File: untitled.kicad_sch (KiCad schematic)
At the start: 2 parts, among them J1 USB4056-03-A_REVA2, U1 STM32H745ZIT6

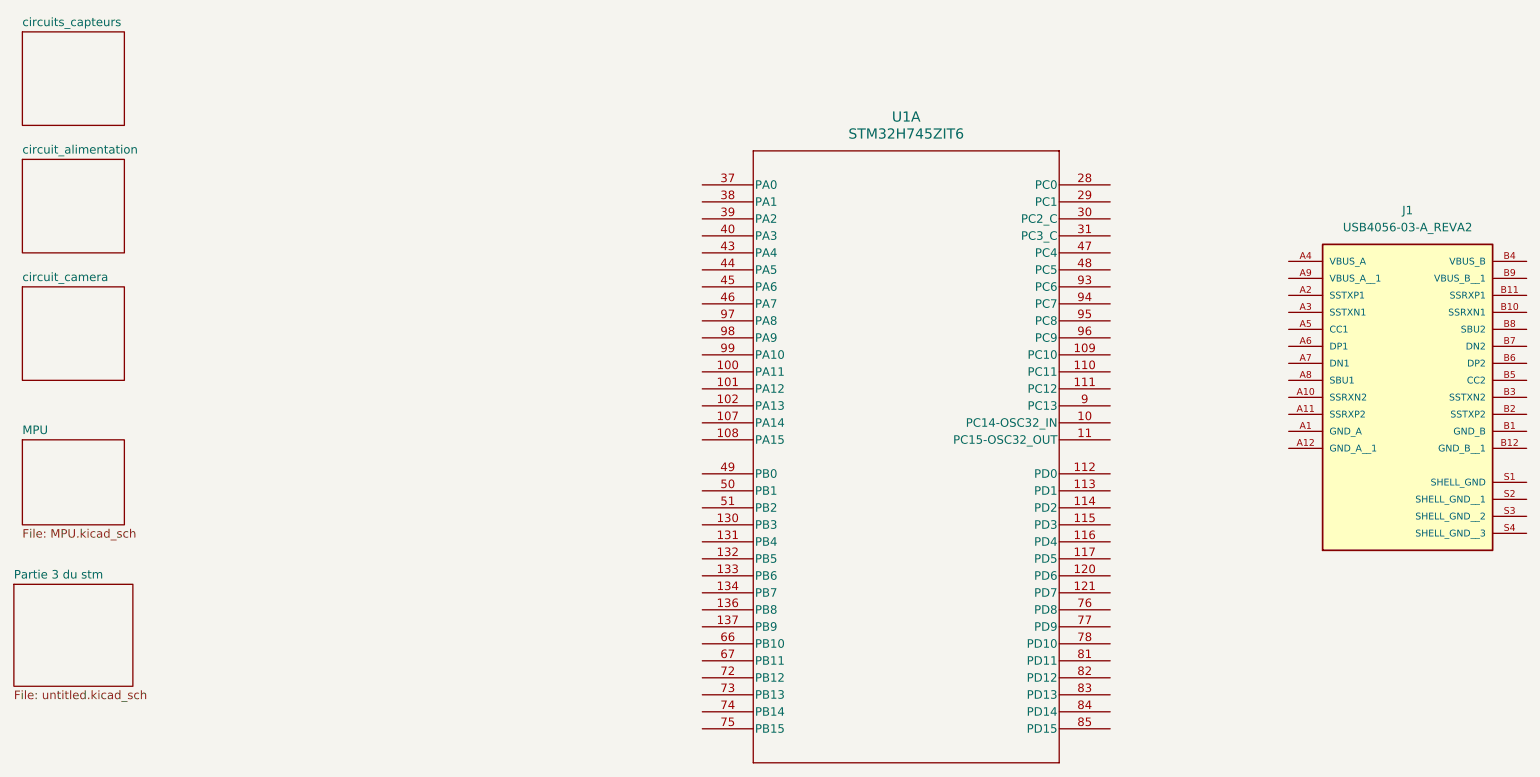
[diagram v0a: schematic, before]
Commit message: Placement de toutes les parties du stm32 dans leur pages respectives
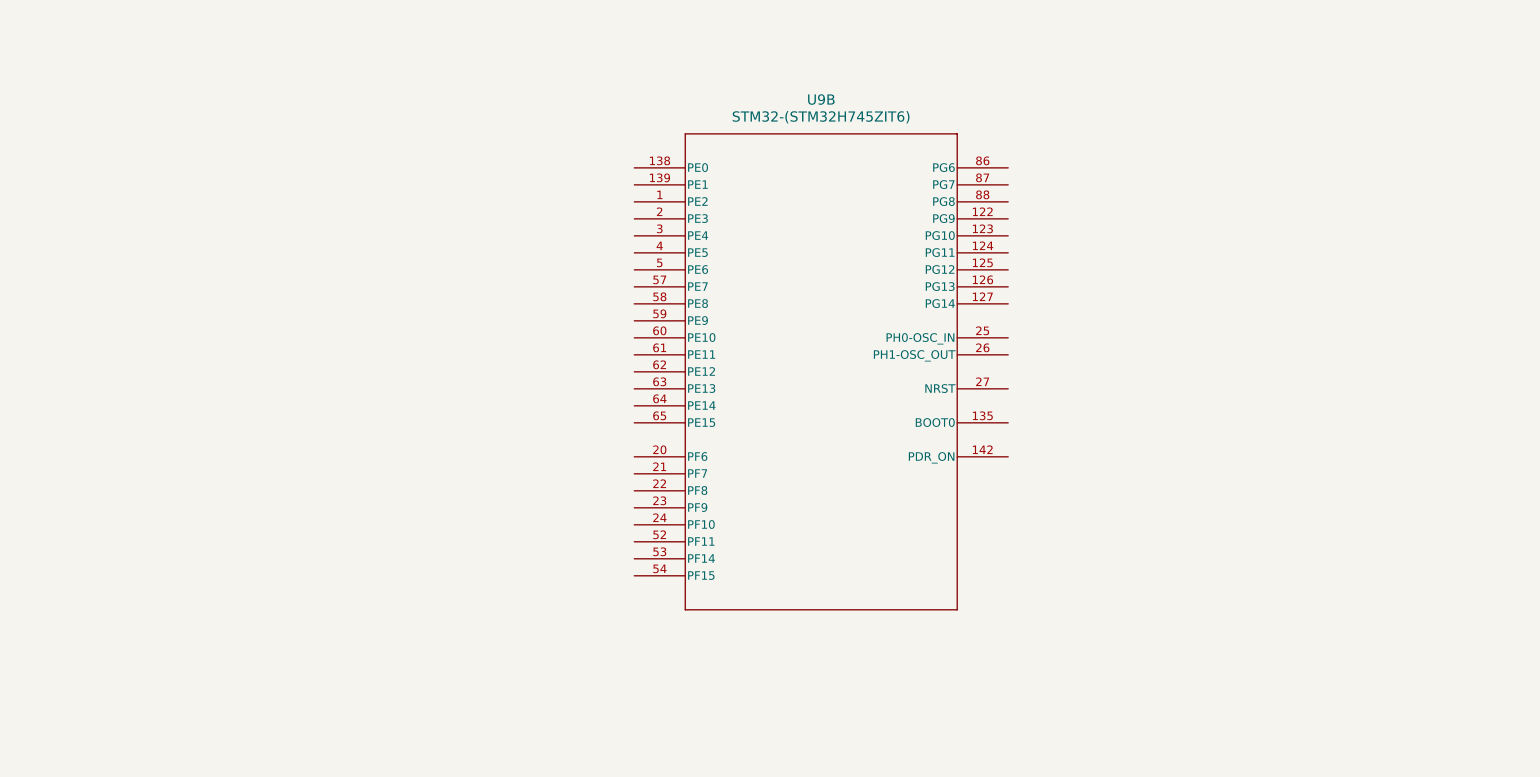
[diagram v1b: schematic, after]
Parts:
- removed J1: USB4056-03-A_REVA2, USB4056-03-A_REVA2:GCT_USB4056-03-A_REVA2, symbol GAUL-Symboles:USB4056-03-A_REVA2
- removed U1: STM32H745ZIT6, LQFP-144, symbol GAUL-Symboles:STM32H745ZIT6
- added U9: STM32-(STM32H745ZIT6), LQFP-144, symbol GAUL-Symboles:STM32-(STM32H745ZIT6)
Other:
- removed sheet MPU
- removed sheet Partie 3 du stm
- removed sheet circuit_alimentation
- removed sheet circuit_camera
- removed sheet circuits_capteurs
- company: GAUL -> (none)
- title: Payload -> (none)
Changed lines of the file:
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@@
 (kicad_sch (version 20230121) (generator eeschema)
   (paper "A4")
-  (title_block
-    (title "Payload")
-    (date "2024-01-29")
-    (rev "0")
-    (company "GAUL")
-  )
-  (symbol (lib_id "GAUL-Symboles:STM32H745ZIT6") (at 118.11 59.69 0) (unit 1)
+  (symbol (lib_id "GAUL-Symboles:STM32-(STM32H745ZIT6)") (at 107.95 57.15 0) (unit 2)
     (in_bom yes) (on_board yes) (dnp no) (fields_autoplaced)
-    (property "Reference" "U1" (at 148.59 49.53 0)
+    (property "Reference" "U9" (at 135.89 46.99 0)
       (effects (font (size 1.524 1.524)))
     )
-    (property "Value" "STM32H745ZIT6" (at 148.59 52.07 0)
+    (property "Value" "STM32-(STM32H745ZIT6)" (at 135.89 49.53 0)
       (effects (font (size 1.524 1.524)))
     )
-    (property "Footprint" "LQFP-144" (at 118.11 59.69 0)
+    (property "Footprint" "LQFP-144" (at 107.95 57.15 0)
       (effects (font (size 1.27 1.27) italic) hide)
     )
-    (property "Datasheet" "STM32H745ZIT6" (at 118.11 59.69 0)
+    (property "Datasheet" "STM32H745ZIT6" (at 107.95 57.15 0)
       (effects (font (size 1.27 1.27) italic) hide)
     )
@@
     (instances
       (project "Payload"
-        (path "/5f62c44b-34ee-4720-b187-b4a520863a8a"
-          (reference "U1") (unit 1)
+        (path "/5f62c44b-34ee-4720-b187-b4a520863a8a/b20c1a40-233f-480d-ac91-6f1a7bcdc93c"
+          (reference "U9") (unit 2)
+        )
+        (path "/5f62c44b-34ee-4720-b187-b4a520863a8a/eebde64d-8ea7-44c4-a899-54cec4ec467f"
+          (reference "U9") (unit 2)
         )
       )
     )
   )
-  (symbol (lib_id "GAUL-Symboles:USB4056-03-A_REVA2") (at 223.52 83.82 0) (unit 1)
-    (in_bom yes) (on_board yes) (dnp no) (fields_autoplaced)
-    (property "Reference" "J1" (at 223.52 63.5 0)
-      (effects (font (size 1.27 1.27)))
-    )
-    (property "Value" "USB4056-03-A_REVA2" (at 223.52 66.04 0)
-      (effects (font (size 1.27 1.27)))
-    )
-    (property "Footprint" "USB4056-03-A_REVA2:GCT_USB4056-03-A_REVA2" (at 223.52 83.82 0)
-      (effects (font (size 1.27 1.27)) (justify bottom) hide)
-    )
-    (property "Datasheet" "" (at 223.52 83.82 0)
-      (effects (font (size 1.27 1.27)) hide)
-    )
-    (property "PARTREV" "A2" (at 223.52 83.82 0)
-      (effects (font (size 1.27 1.27)) (justify bottom) hide)
-    )
-    (property "STANDARD" "Manufacturer Recommendations" (at 223.52 83.82 0)
-      (effects (font (size 1.27 1.27)) (justify bottom) hide)
-    )
-    (property "SNAPEDA_PN" "USB4056-03-A" (at 223.52 83.82 0)
-      (effects (font (size 1.27 1.27)) (justify bottom) hide)
-    )
-    (property "MAXIMUM_PACKAGE_HEIGHT" "3.31 mm" (at 223.52 83.82 0)
-      (effects (font (size 1.27 1.27)) (justify bottom) hide)
-    )
-    (property "MANUFACTURER" "GCT" (at 223.52 83.82 0)
-      (effects (font (size 1.27 1.27)) (justify bottom) hide)
-    )
-    (pin "A1")
-    (pin "A10")
-    (pin "A11")
-    (pin "A12")
-    (pin "A2")
-    (pin "A3")
-    (pin "A4")
-    (pin "A5")
-    (pin "A6")
-    (pin "A7")
-    (pin "A8")
-    (pin "A9")
-    (pin "B1")
-    (pin "B10")
-    (pin "B11")
-    (pin "B12")
-    (pin "B2")
-    (pin "B3")
-    (pin "B4")
-    (pin "B5")
-    (pin "B6")
-    (pin "B7")
-    (pin "B8")
-    (pin "B9")
-    (pin "S1")
-    (pin "S2")
-    (pin "S3")
-    (pin "S4")
-    (instances
-      (project "Payload"
-        (path "/5f62c44b-34ee-4720-b187-b4a520863a8a"
-          (reference "J1") (unit 1)
-        )
-      )
-    )
-  )
-  (sheet (at 16.51 36.83) (size 15.24 13.97) (fields_autoplaced)
-    (stroke (width 0.1524) (type solid))
-    (fill (color 0 0 0 0.0000))
-    (property "Sheetname" "circuits_capteurs" (at 16.51 36.1184 0)
-      (effects (font (size 1.27 1.27)) (justify left bottom))
-    )
-    (property "Sheetfile" "circuits_capteurs.kicad_sch" (at 16.51 51.3846 0)
-      (effects (font (size 1.27 1.27)) (justify left top) hide)
-    )
-    (instances
-      (project "Payload"
-        (path "/5f62c44b-34ee-4720-b187-b4a520863a8a" (page "2"))
-      )
-    )
-  )
-  (sheet (at 16.51 55.88) (size 15.24 13.97) (fields_autoplaced)
-    (stroke (width 0.1524) (type solid))
-    (fill (color 0 0 0 0.0000))
-    (property "Sheetname" "circuit_alimentation" (at 16.51 55.1684 0)
-      (effects (font (size 1.27 1.27)) (justify left bottom))
-    )
-    (property "Sheetfile" "circuit_alimentation.kicad_sch" (at 16.51 70.4346 0)
-      (effects (font (size 1.27 1.27)) (justify left top) hide)
-    )
-    (instances
-      (project "Payload"
-        (path "/5f62c44b-34ee-4720-b187-b4a520863a8a" (page "3"))
-      )
-    )
-  )
-  (sheet (at 16.51 74.93) (size 15.24 13.97) (fields_autoplaced)
-    (stroke (width 0.1524) (type solid))
-    (fill (color 0 0 0 0.0000))
-    (property "Sheetname" "circuit_camera" (at 16.51 74.2184 0)
-      (effects (font (size 1.27 1.27)) (justify left bottom))
-    )
-    (property "Sheetfile" "circuit_camera.kicad_sch" (at 16.51 89.4846 0)
-      (effects (font (size 1.27 1.27)) (justify left top) hide)
-    )
-    (instances
-      (project "Payload"
-        (path "/5f62c44b-34ee-4720-b187-b4a520863a8a" (page "4"))
-      )
-    )
-  )
-  (sheet (at 16.51 97.79) (size 15.24 12.7) (fields_autoplaced)
-    (stroke (width 0.1524) (type solid))
-    (fill (color 0 0 0 0.0000))
-    (property "Sheetname" "MPU" (at 16.51 97.0784 0)
-      (effects (font (size 1.27 1.27)) (justify left bottom))
-    )
-    (property "Sheetfile" "MPU.kicad_sch" (at 16.51 111.0746 0)
-      (effects (font (size 1.27 1.27)) (justify left top))
-    )
-    (instances
-      (project "Payload"
-        (path "/5f62c44b-34ee-4720-b187-b4a520863a8a" (page "5"))
-      )
-    )
-  )
-  (sheet (at 15.24 119.38) (size 17.78 15.24) (fields_autoplaced)
-    (stroke (width 0.1524) (type solid))
-    (fill (color 0 0 0 0.0000))
-    (property "Sheetname" "Partie 3 du stm" (at 15.24 118.6684 0)
-      (effects (font (size 1.27 1.27)) (justify left bottom))
-    )
-    (property "Sheetfile" "untitled.kicad_sch" (at 15.24 135.2046 0)
-      (effects (font (size 1.27 1.27)) (justify left top))
-    )
-    (instances
-      (project "Payload"
-        (path "/5f62c44b-34ee-4720-b187-b4a520863a8a" (page "6"))
-      )
-    )
-  )
-  (sheet_instances
-    (path "/" (page "1"))
-  )
 )
